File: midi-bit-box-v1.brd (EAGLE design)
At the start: 109.9 x 59.1 mm, 52 parts, among them IC1 LM386, IC2 CD4024BE, T1 42TM011-RC, U1 AY-3-8910

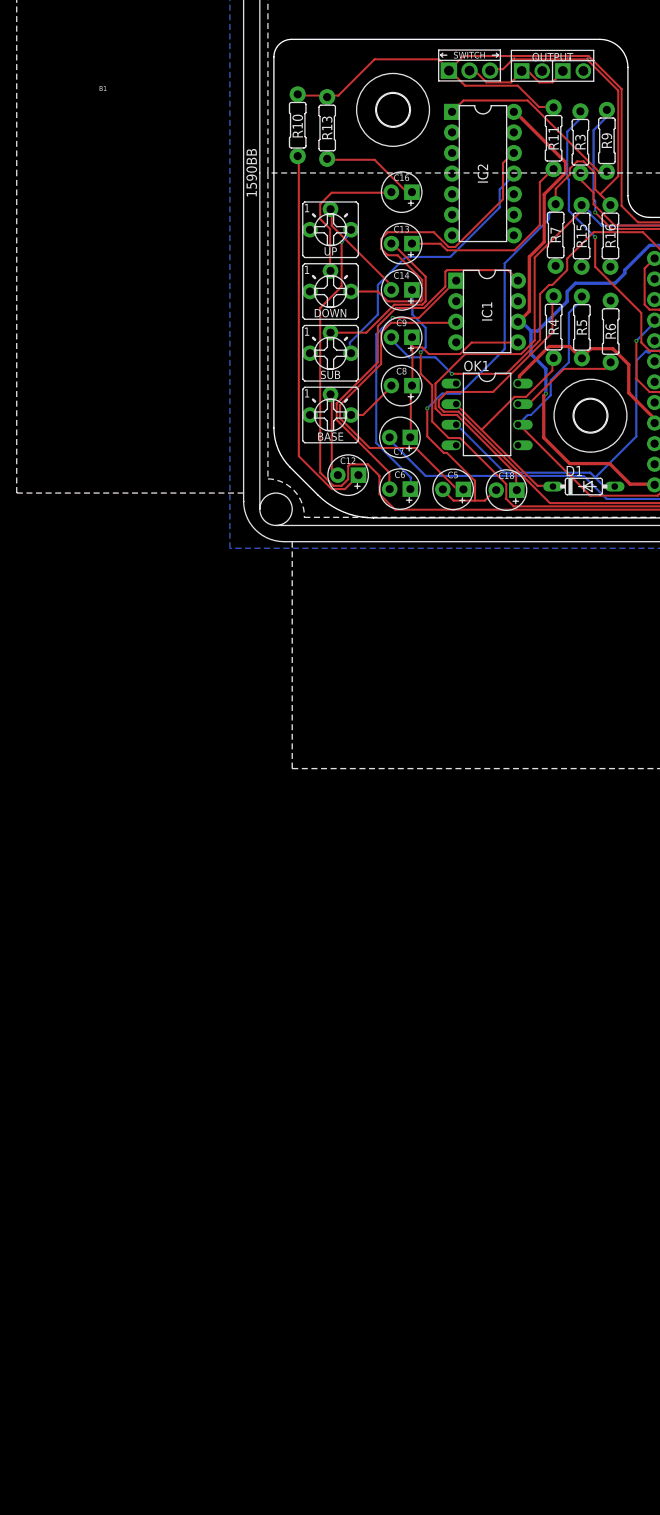
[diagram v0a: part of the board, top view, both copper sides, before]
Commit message: Added SPST and latching relay switching circuit
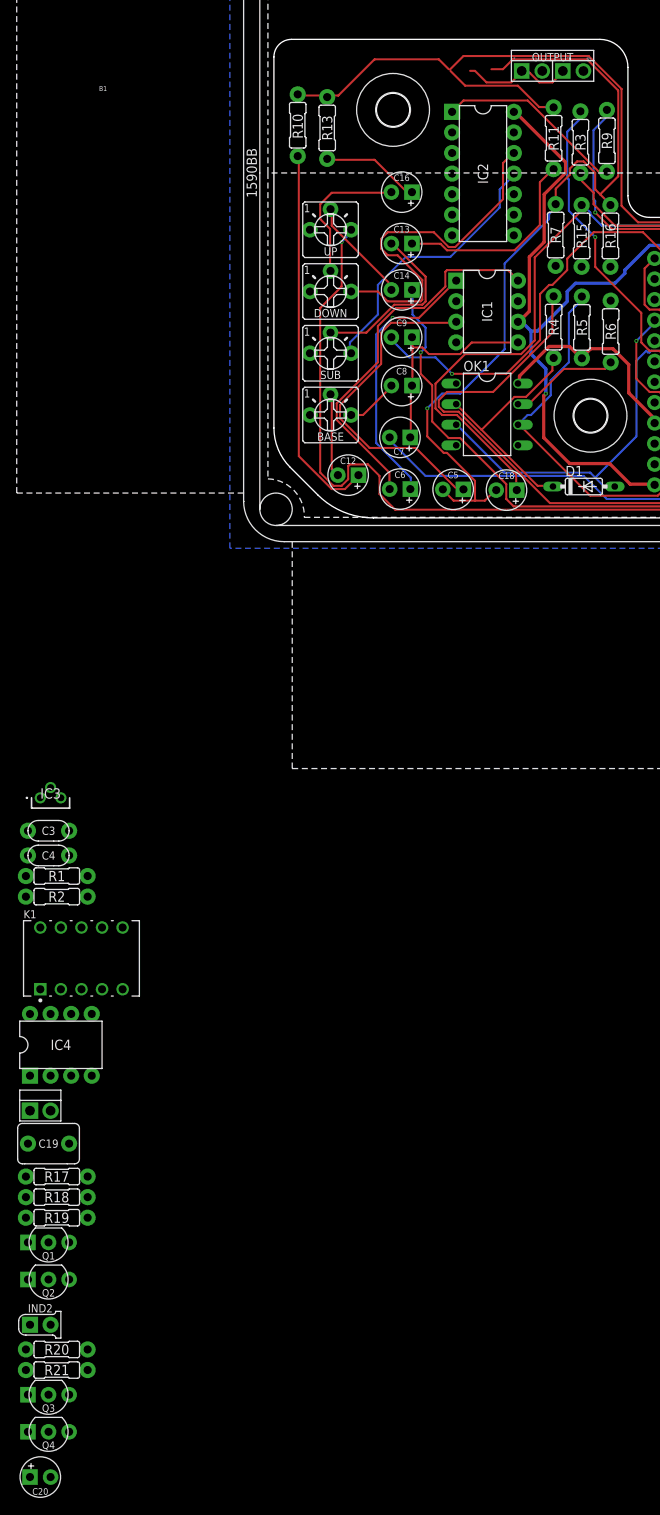
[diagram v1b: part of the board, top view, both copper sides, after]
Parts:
- removed SWITCH: (no value), switches:SPDT.WIRE
- added BLAST: SPST, switches:SPST.WIRE
- added C19: 1uF, caps-film:0.2".LRG
- added C20: 100uF, caps-elec:0502
- added C3, C4: 100nF, caps-film:0.2".SML
- added IC3: 78L09, SamacSys_Parts:L78L09ACZTR
- added IC4: NE555, integrated circuits:DIP08
- added IND2: 5MM_LED, diodes:3MM_1
- added K1: PANASONIC_TQ2-L-5VPANASONIC_TQ2-L-5V_0_0, Panasonic - TQ2-L-5V:PANASONIC_TQ2-L-5V_0
- added Q1, Q2, Q3: 2N3904, transistors-BJT:TO92
- added Q4: 2N3906, transistors-BJT:TO92
- added R1, R2: (no value), resistors:0.3".B
- added R17: 100K, resistors:0.3".B
- added R18, R19, R21: 10K, resistors:0.3".B
- added R20: 4.7K, resistors:0.3".B
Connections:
- removed net N$49: R10.2, R11.2, R12.2, R13.2, SWITCH.1
- new net N$40: BLAST.2, C19.2, R17.2
- new net N$50: IND2.A, R20.2
- new net N$51: Q2.1, R21.1
- new net N$52: Q2.2, R18.1
- new net N$53: Q1.2, R19.1
- new net N$54: IND2.K, Q1.1
- new net N$55: C20.+, Q3.3, Q4.3
- new net N$56: Q3.2, Q4.2
- new net N$57: C20.-, K1.1
- new net N$58: C18.-, K1.2, K1.7, R16.2
- new net N$59: K1.9, R10.2, R11.2, R12.2, R13.2
- new net N$7: IC4.3, R17.1, R18.2, R19.2
- new net VC: C4.1, IC3.1, IC4.4, IC4.8, Q3.1, R1.2, R20.1, R21.2
- new net VD: BLAST.1, IC4.2, IC4.6, R1.1, R2.2
- net GND: now also C19.1, C3.2, C4.2, IC3.2, IC4.1, K1.10, K1.4, Q1.3, Q2.3, Q4.1, R2.1
- net N$45: now also K1.3; no longer C18.-, R16.2, SWITCH.3
- net N$8: now also K1.8; no longer SWITCH.2
- net VA: now also C3.1, IC3.3
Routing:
- net N$49: track 138.7 -> 0.00 mm, vias 1 -> 0
- net N$59: track 0.00 -> 138.1 mm, vias 0 -> 1
- net N$45: track 100.6 -> 100.0 mm
